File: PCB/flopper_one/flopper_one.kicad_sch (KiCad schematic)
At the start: 23 parts, among them J1 To PN532 ->, J2 <- ST7789, Q1 2N2219, SW1 SW_Omron_B3FS, SW2 SW_Omron_B3FS, SW3 SW_Omron_B3FS, SW4 SW_Omron_B3FS, SW5 SW_Omron_B3FS, SW6 SW_SPST, U1 TP4056-42-ESOP8, U4 hw-045

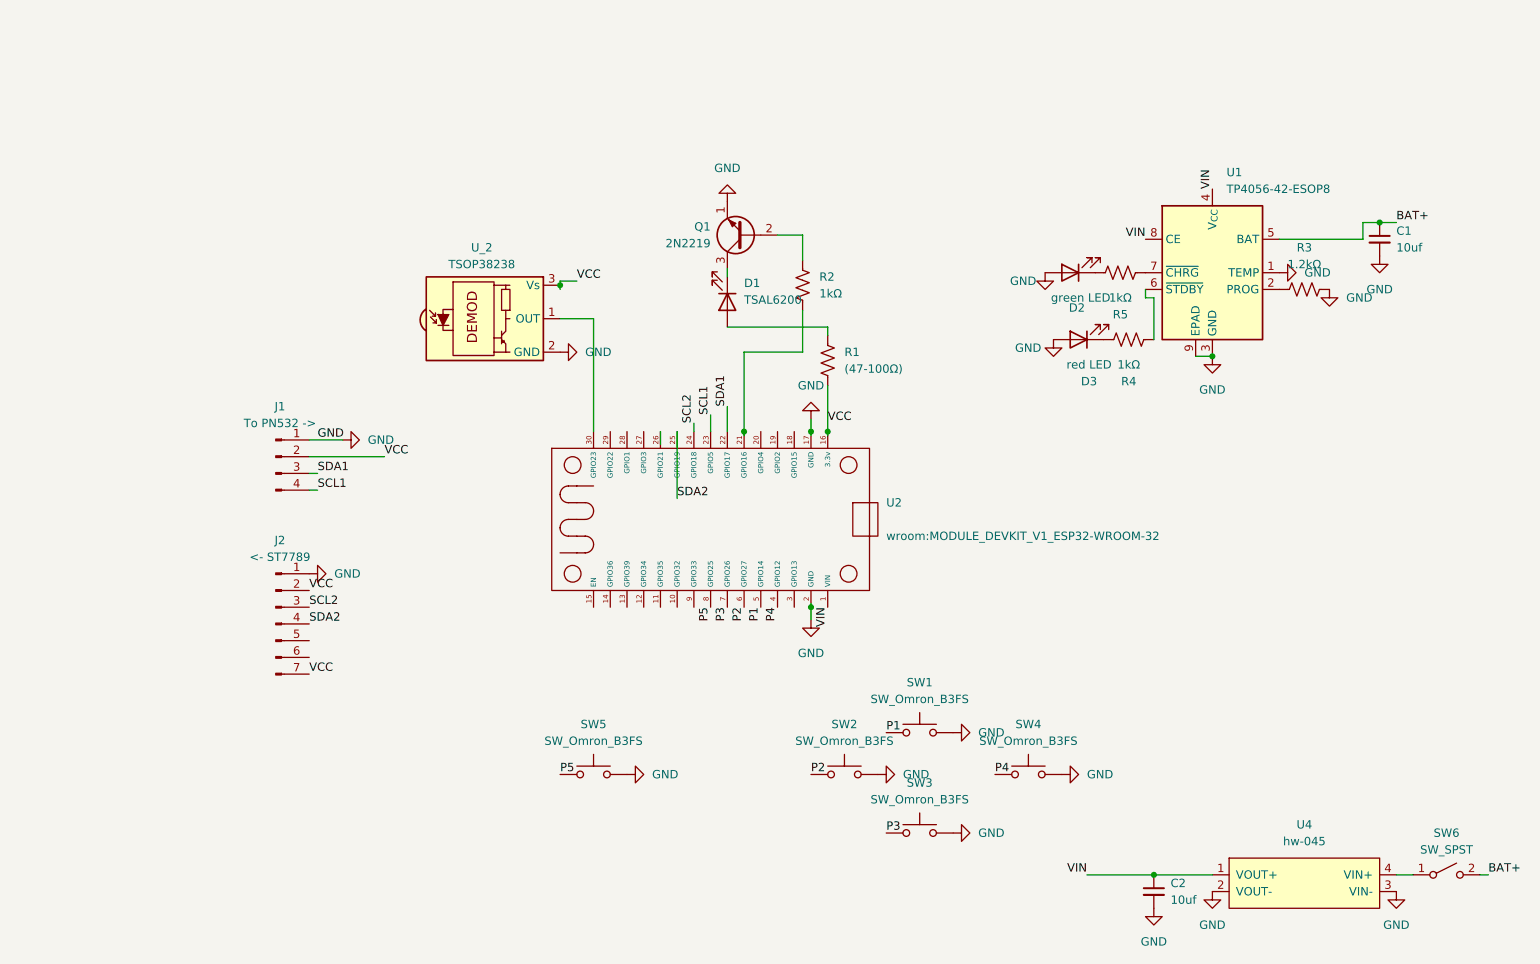
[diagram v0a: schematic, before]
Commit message: move stuff around
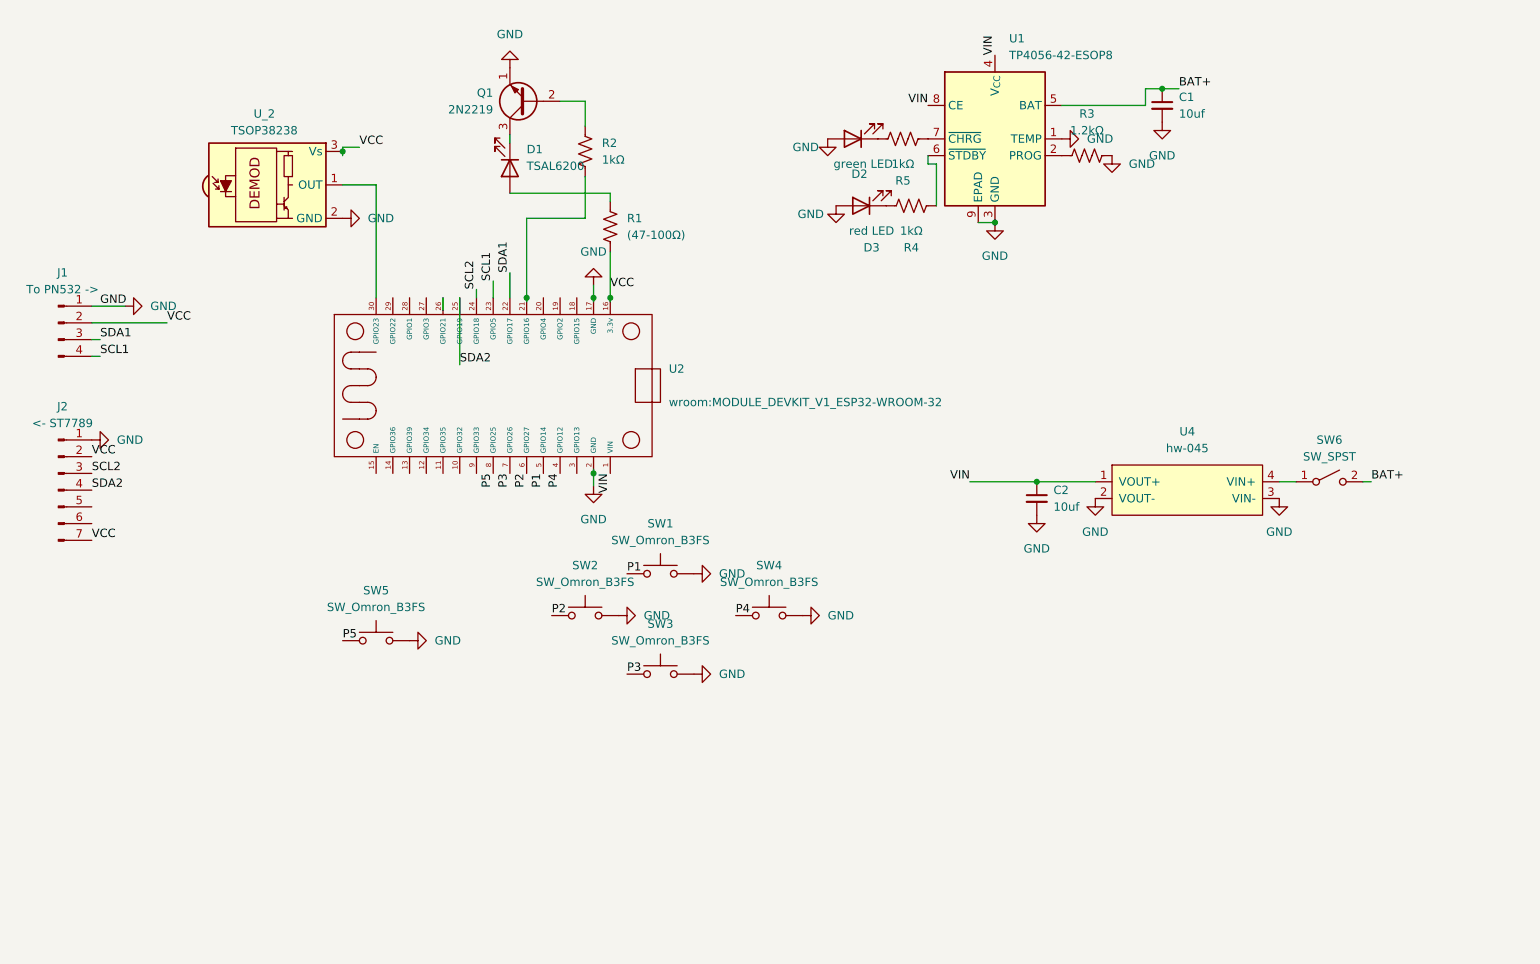
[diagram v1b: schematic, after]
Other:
- moved on the sheet: C1, C2, D1, D2, D3, J1, J2, Q1, R1, R2, R3, R4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

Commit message: "quick" schematic fix
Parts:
- added R6: 0.4Ω, Resistor_THT:R_Axial_DIN0207_L6.3mm_D2.5mm_P7.62mm_Horizontal, symbol Device:R_US
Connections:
- net GND: no longer D2.2 (A), D3.2 (A)
- net VIN: now also R6.1; no longer C2.1, U1.4 (V_{CC}), U1.8 (CE)
- new net: C2.1, D2.2 (A), D3.2 (A), R6.2, U1.4 (V_{CC}), U1.8 (CE)
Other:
- moved on the sheet: C2

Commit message: make thicker and add gnd pour
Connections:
- net CE: now reaches C2.1, D2.2 (A), D3.2 (A), R6.2, U1.4 (V_{CC}), U1.8 (CE)
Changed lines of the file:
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@@
+		)
+	)
+	(label "CE"
+		(at 162.56 24.13 180)
+		(effects
+			(font
+				(size 1.27 1.27)
+			)
+			(justify right bottom)
 		)
 	)
@@
 		(effects
 			(font
+				(size 1.27 1.27)
+			)
+			(justify left bottom)
+		)
+	)
+	(label "tp_vcc"
+		(at 172.72 16.51 0)
+		(effects
+			(font

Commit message: adfadfds
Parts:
- removed R6: 0.4Ω, Resistor_THT:R_Axial_DIN0207_L6.3mm_D2.5mm_P7.62mm_Horizontal, symbol Device:R_US
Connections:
- net VIN is gone; now on net CE: U2.1 (VIN), U4.1 (VOUT+)
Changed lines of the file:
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@@
 	(wire
 		(pts
-			(xy 142.24 17.78) (xy 140.97 17.78)
-		)
-		(stroke
-			(width 0)
-			(type default)
-		)
-	)
-	(wire
-		(pts
 			(xy 99.06 28.575) (xy 99.06 29.845)
 		)
@@
 	(wire
 		(pts
+			(xy 133.35 17.78) (xy 142.24 17.78)
+		)
+		(stroke
+			(width 0)
+			(type default)
+		)
+	)
+	(wire
+		(pts
 			(xy 35.56 59.69) (xy 36.83 59.69)
 		)
@@
 		(on_board yes)
 		(dnp no)
-		(fields_autoplaced yes)
 		(property "Reference" "R3"
 			(at 186.69 25.4 90)
@@
 		)
 		(property "Value" "1.2kΩ"
-			(at 186.69 27.94 90)
+			(at 186.436 33.782 90)
 			(effects
 				(font
@@
 					(unit 1)
 				)
-			)
-		)
-	)
-	(symbol
-		(lib_id "Device:R_US")
-		(at 137.16 17.78 90)
-		(unit 1)
-		(exclude_from_sim no)
-		(in_bom yes)
-		(on_board yes)
-		(dnp no)
-		(fields_autoplaced yes)
-		(property "Reference" "R6"
-			(at 137.16 11.43 90)
-			(effects
-				(font
-					(size 1.27 1.27)
-				)
-			)
-		)
-		(property "Value" "0.4Ω"
-			(at 137.16 13.97 90)
-			(effects
-				(font
-					(size 1.27 1.27)
-				)
-			)
-		)
-		(property "Footprint" "Resistor_THT:R_Axial_DIN0207_L6.3mm_D2.5mm_P7.62mm_Horizontal"
-			(at 137.414 16.764 90)
-			(effects
-				(font
-					(size 1.27 1.27)
-				)
-				(hide yes)
-			)
-		)
-		(property "Datasheet" "~"
-			(at 137.16 17.78 0)
-			(effects
-				(font
-					(size 1.27 1.27)
-				)
-				(hide yes)
-			)
-		)
-		(property "Description" "Resistor, US symbol"
-			(at 137.16 17.78 0)
-			(effects
-				(font
-					(size 1.27 1.27)
-				)
-				(hide yes)
-			)
-		)
-		(pin "1"
-		)
-		(pin "2"
-		)
-		(instances
-			(project ""
-				(path "/8fc37294-f81b-4810-89c7-f789c9f89558"
-					(reference "R6")
-					(unit 1)
-				)

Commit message: display is spi oops
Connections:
- net DC: now reaches U2.10 (GPIO32)
- net DC: now also J2.6 (Pin_6)
- net RES: now reaches U2.9 (GPIO33)
- net RES: now also J2.5 (Pin_5)
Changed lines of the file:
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@@
+		)
+	)
+	(label "DC"
+		(at 91.44 80.01 270)
+		(effects
+			(font
+				(size 1.27 1.27)
+			)
+			(justify right bottom)
 		)
 	)
@@
 	(label "BAT+"
 		(at 229.87 81.28 0)
+		(effects
+			(font
+				(size 1.27 1.27)
+			)
+			(justify left bottom)
+		)
+	)
+	(label "RES"
+		(at 35.56 85.09 0)
 		(effects
 			(font
@@
 	(label "SCL1"
 		(at 96.52 50.8 90)
+		(effects
+			(font
+				(size 1.27 1.27)
+			)
+			(justify left bottom)
+		)
+	)
+	(label "DC"
+		(at 35.56 87.63 0)
 		(effects
 			(font
@@
 		)
 	)
+	(label "RES"
+		(at 93.98 80.01 270)
+		(effects
+			(font
+				(size 1.27 1.27)
+			)
+			(justify right bottom)
+		)
+	)

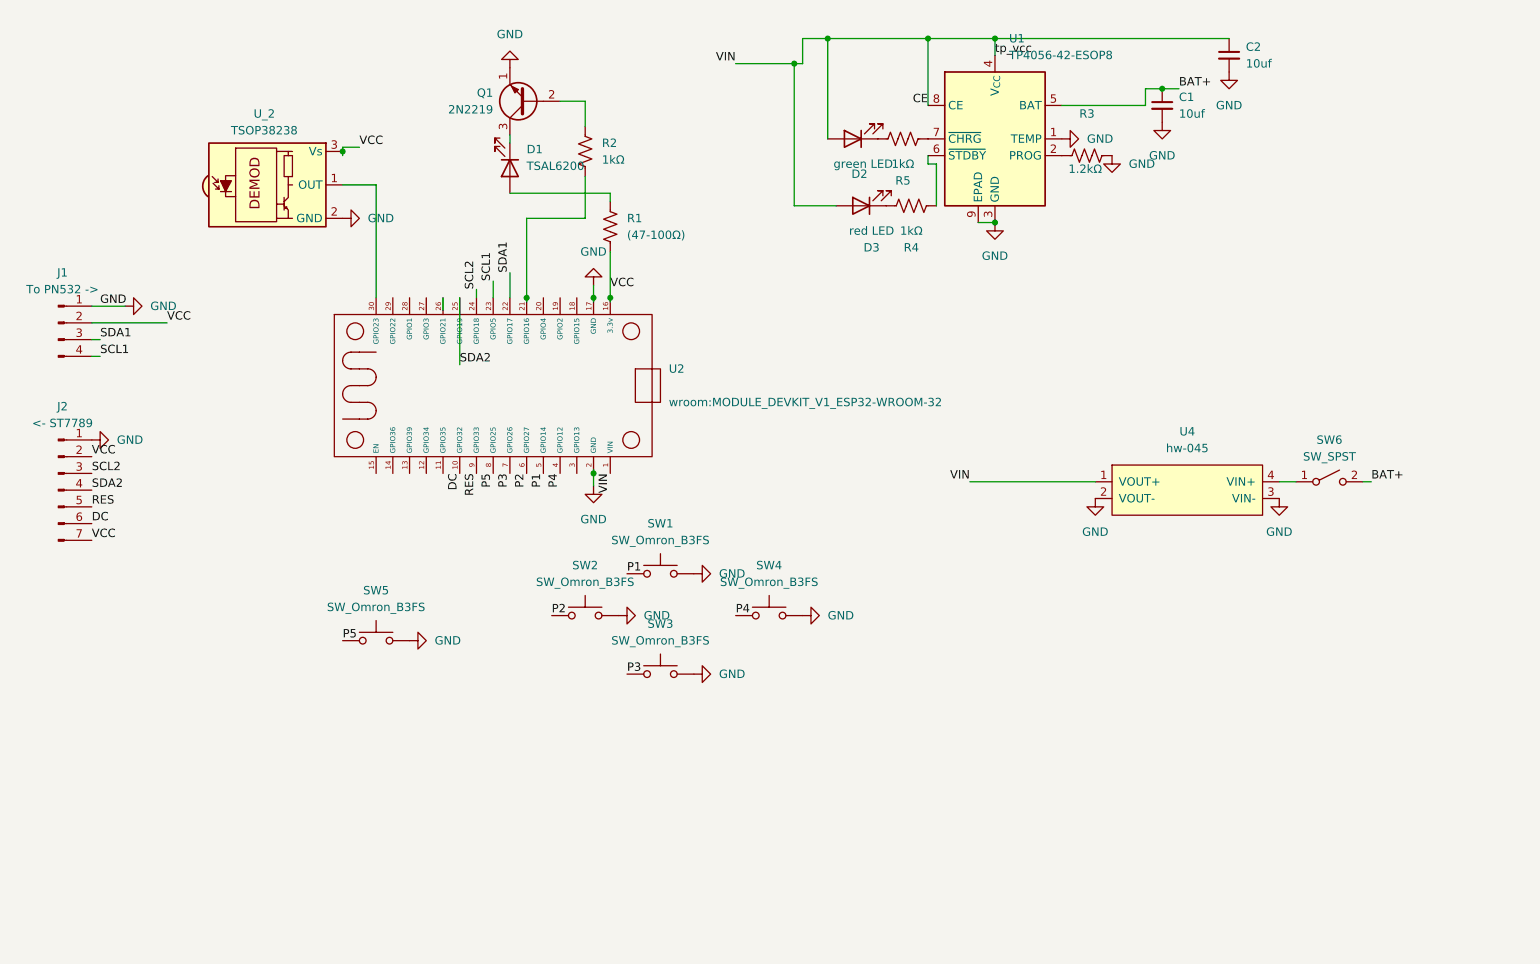
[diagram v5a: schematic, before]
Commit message: simplify a bunch because reordering pcb
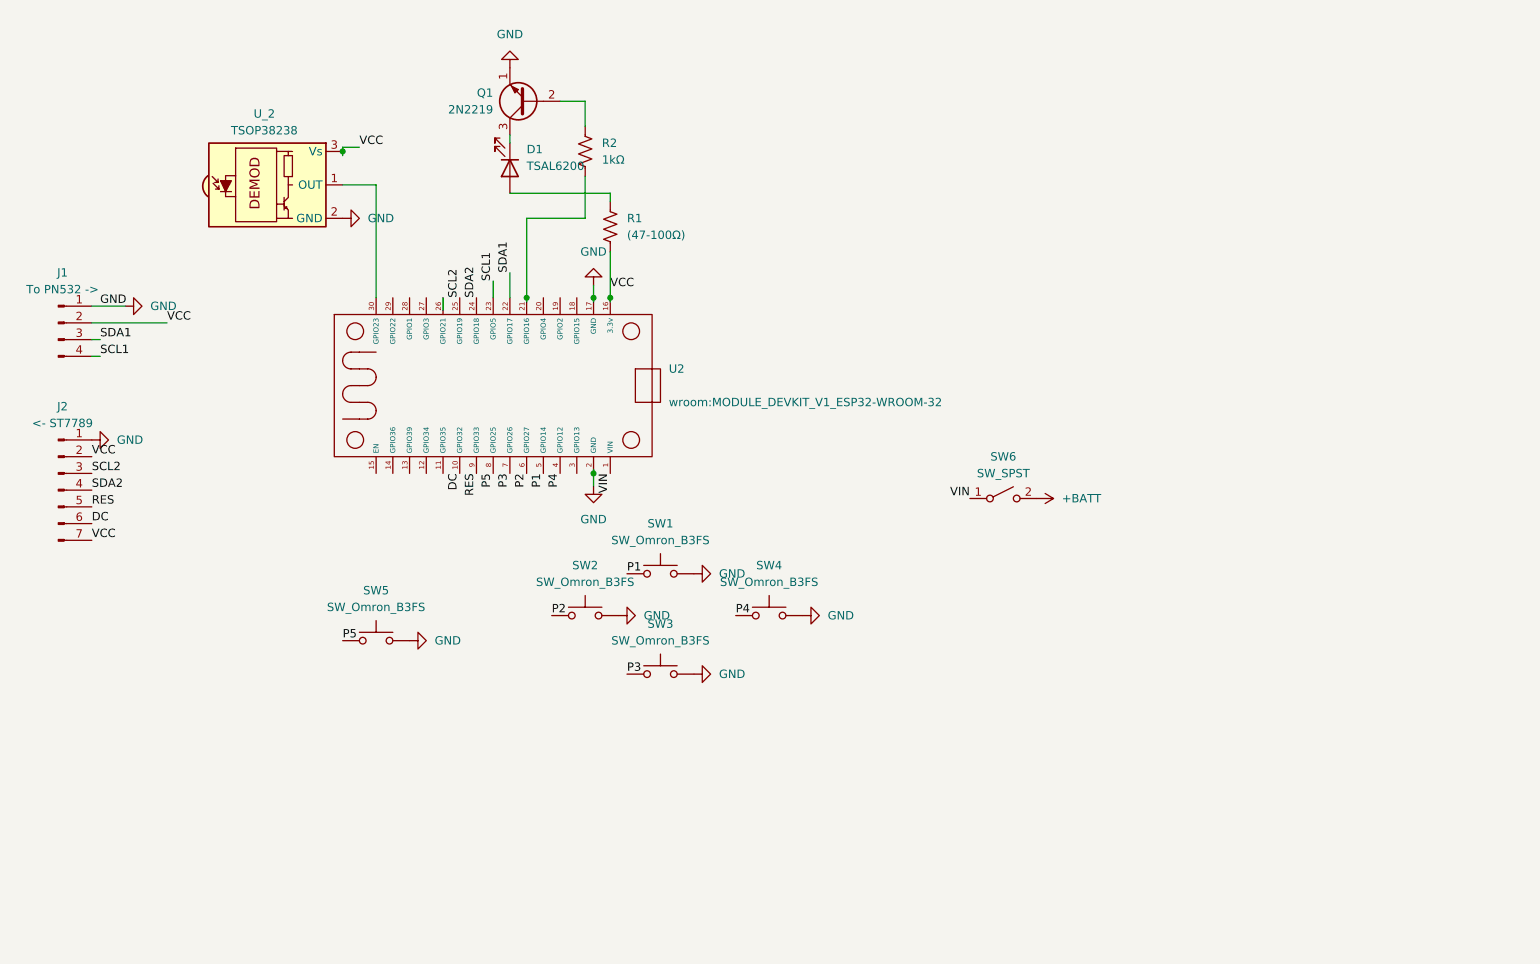
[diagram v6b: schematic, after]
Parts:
- removed C1, C2: 10uf, Capacitor_THT:CP_Axial_L10.0mm_D4.5mm_P15.00mm_Horizontal, symbol Device:C_Small
- removed D2: green LED, LED_THT:LED_D5.0mm, symbol Device:LED
- removed D3: red LED, LED_THT:LED_D5.0mm, symbol Device:LED
- removed R3: 1.2kΩ, Resistor_THT:R_Axial_DIN0207_L6.3mm_D2.5mm_P7.62mm_Horizontal, symbol Device:R_US
- removed R4, R5: 1kΩ, Resistor_THT:R_Axial_DIN0207_L6.3mm_D2.5mm_P7.62mm_Horizontal, symbol Device:R_US
- removed U1: TP4056-42-ESOP8, Package_SO:SOIC-8-1EP_3.9x4.9mm_P1.27mm_EP2.41x3.3mm_ThermalVias, symbol Battery_Management:TP4056-42-ESOP8
- removed U4: hw-045, MT3608:hw-045, symbol hw-045:hw-045
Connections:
- net CE is gone; now on net VIN: U2.1 (VIN)
- net SCL2: now also U2.25 (GPIO19); no longer U2.24 (GPIO18)
- net SDA2: now also U2.24 (GPIO18); no longer U2.25 (GPIO19)
- net VIN: now reaches SW6.1 (A)
- net BAT+ renamed +BATT
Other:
- moved on the sheet: SW6
